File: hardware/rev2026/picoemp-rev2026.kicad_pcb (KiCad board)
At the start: 2 copper layers, 40 x 130 mm, 53 parts, among them J1 EDGE-SMA, J2 1x2_Pin_Header, J3 MKDS 1,5/2-5.08, J4 EDGE-SMA, P1 Header 7, P2 Header 2, P3 Header 4, Q1 LDA111STR, Q2 RGT16BM65DTL, Q3 AO3422, Q4 AO3422, SW1 KSC741J LFS, SW2 KSC741J LFS, SW3 TL3301AF160QJ, T1 ATB322524, T2 ATB322524, U1 SC0915, U2 74LVC1G17

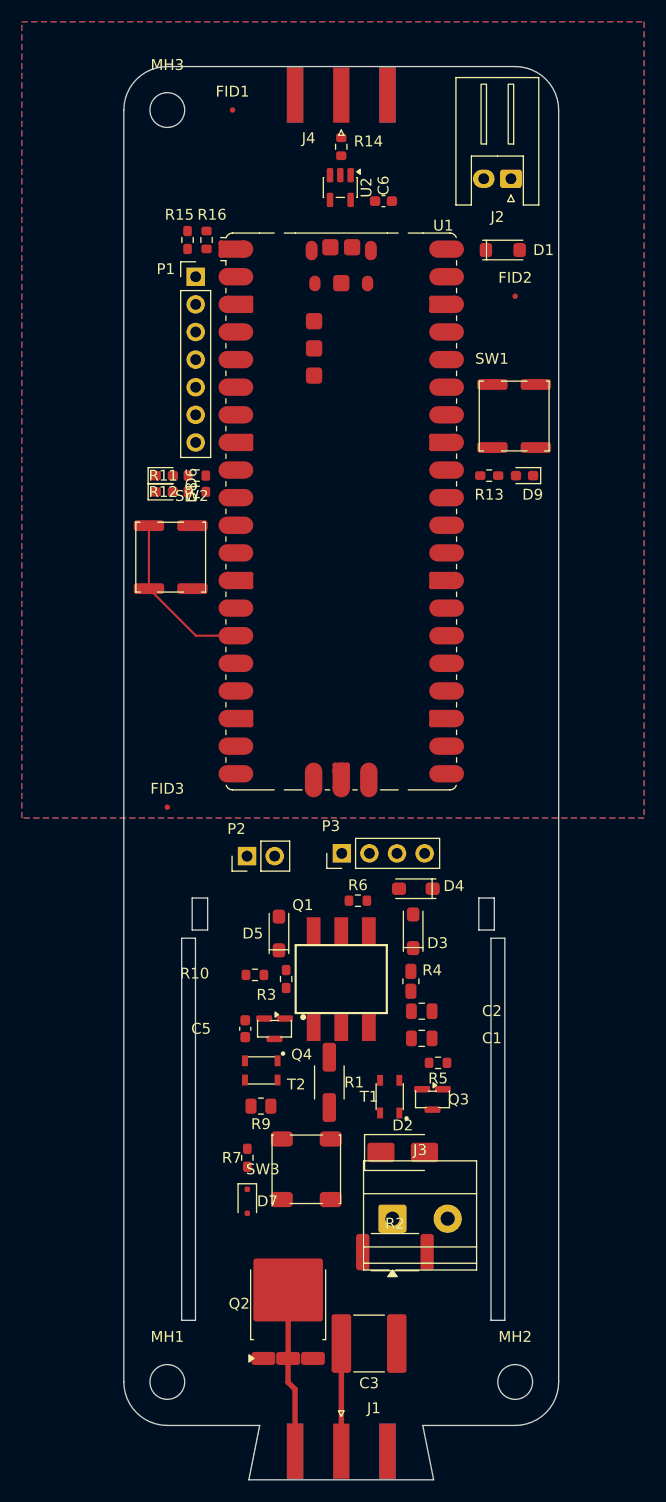
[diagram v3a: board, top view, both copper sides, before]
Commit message: Cut a USB notch in the north edge; J4 east; rearrange the north end
The Pico's USB faces north with 13.6 mm of board in front of it. The connector
centreline sits ~1.5 mm above our board surface, so a micro-B plug body -- ~6 mm
tall, centred -- would need to occupy space 1.5 mm BELOW the board. It cannot be
inserted at all. Moving J4 alone would not have fixed this; the plug is the
problem, not the SMA.

Chose a notch over moving the Pico north. Moving it up sounds cleaner and frees
enough length to shorten the board back toward 116 mm, but the module is 23 mm
wide and the usable north edge is only 32 mm, so the Pico would occupy all but
~4.5 mm at each end and J4 -- which must be at rot +/-90 -- would have nowhere to
go. Pico-north fixes the USB by breaking the trigger SMA. The notch fixes both.

  notch          x 118.39..130.39, y 19.872..33.0   centred on the USB
  west strip     x 108.39..118.39  10.00 mm         R14, U2, C6, D1, MH3, FID1
  east strip     x 130.39..143.12  12.73 mm         J4 (1.36 mm each side), J2

The north-east corner radius drops 4.000 -> 1.270 to make that east strip fit.
R=4.000 exists to be concentric with a mounting hole, and the north-east corner
has none, so it was the only radius that could be conceded without losing what
the radius was for. The other three keep it.

J4 is DNP -- an optional trigger input -- so where the two competed, the USB won
and J4 took the compromise. It still lands with 1.36 mm of margin.

MH3 is NOT centred at the top as asked: that is exactly where the USB notch has
to go. It stays concentric in the north-west corner instead.

Two placement attempts were backed out before this one. Shifting the Pico 1 mm
west to centre the notch on it cascaded into P1/R11/R12/SW2 and shorted SW2 pad 2
to U1 pad 11. Putting the trigger front-end in the east strip left no room for
J2, whose courtyard is 8.4 x 12.5 mm.

DRC back to exactly 7 errors -- every one pre-existing in the HV cluster, none
introduced by this rearrange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
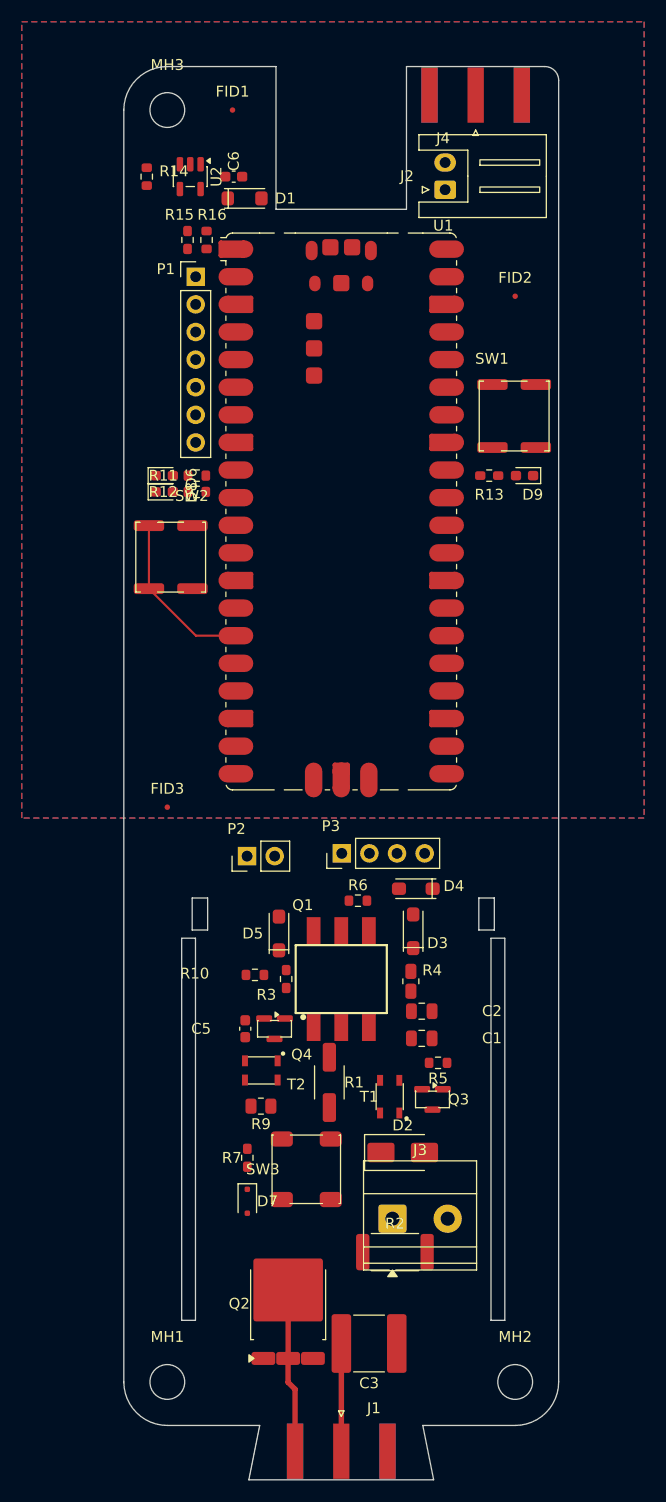
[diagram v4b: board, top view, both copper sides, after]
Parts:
- moved D1 24.2 mm to (115.5, 32.0)
- moved R14 18.1 mm to (106.5, 30.0)
- moved C6 14.0 mm to (114.5, 30.0)
- moved U2 13.8 mm to (110.5, 30.0)
- moved J4 12.4 mm to (136.8, 22.5)
- moved J2 6.14 mm to (133.9, 31.2), turned to 90 degrees
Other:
- outline, holes or cut-outs redrawn
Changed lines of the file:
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@@
 	(footprint "Capacitor_SMD:C_0603_1608Metric"
 		(layer "F.Cu")
-		(at 128.275 32.25)
+		(at 114.5 30)
 		(descr "Capacitor SMD 0603 (1608 Metric), square (rectangular) end terminal, IPC-7351 nominal, (Body size source: IPC-SM-782 page 76, https://www.pcb-3d.com/wordpress/wp-content/uploads/ipc-sm-782a_amendment_1_and_2.pdf)")
 		(tags "capacitor")
@@
 	(footprint "picoemp:D_SOD-123FL"
 		(layer "F.Cu")
-		(at 139.25 36.75)
+		(at 115.5 32)
 		(descr "MCC SOD-123FL (flat lead), e.g. SM4005PL-TP. Pad centres at +/-1.55mm (3.10mm span), size 1.15x1.3mm -- copied from the as-fabricated main:DSS13UTR footprint used for D1 on the original board (a SOD-123FL rectifier), and cross-checked against Central Semiconductor's own SOD-123FL mounting-pad drawing (4.1mm overall pad-to-pad envelope minus a 0.95mm pad width = 3.15mm centre span, within 0.05mm). An earlier draft of this footprint used MCC's suggested-pad-layout figure at 2.36mm; that number turned out to be the INNER-EDGE gap between pads, not the centre-to-centre span, so the earlier pads landed short of the body outline entirely. KiCad's stock Diode_SMD:D_SOD-123F uses a 2.8mm pad span (1.1x1.1mm square pads), which is still off this package's real geometry; use this footprint instead for SOD-123FL parts.")
 		(tags "diode SOD-123FL SOD123FL flat lead")
@@
 	(footprint "Connector_Coaxial:SMA_Amphenol_132289_EdgeMount"
 		(layer "F.Cu")
-		(at 124.39 22.499 90)
+		(at 136.755 22.499 90)
 		(descr "https://www.amphenolrf.com/library/download/link/link_id/595984/parent/132289/")
 		(tags "SMA")
@@
 	(footprint "Connector_JST:JST_XH_S2B-XH-A_1x02_P2.50mm_Horizontal"
 		(layer "F.Cu")
-		(at 140 30.195 180)
+		(at 133.945 31.2 90)
 		(descr "JST XH series connector, S2B-XH-A (http://www.jst-mfg.com/product/pdf/eng/eXH.pdf)")
 		(tags "connector JST XH horizontal")
@@
 	(footprint "Package_TO_SOT_SMD:SOT-23-5"
 		(layer "F.Cu")
-		(at 124.3025 31 -90)
+		(at 110.5 30 -90)
 		(descr "SOT, 5 Pin (JEDEC MO-178 Var AA https://www.jedec.org/document_search?search_api_views_fulltext=MO-178)")
 		(tags "SOT TO_SOT_SMD")
@@
 	(footprint "Resistor_SMD:R_0603_1608Metric"
 		(layer "F.Cu")
-		(at 124.39 27.25 -90)
+		(at 106.5 30 -90)
 		(descr "Resistor SMD 0603 (1608 Metric), square (rectangular) end terminal, IPC-7351 nominal, (Body size source: IPC-SM-782 page 72, https://www.pcb-3d.com/wordpress/wp-content/uploads/ipc-sm-782a_amendment_1_and_2.pdf)")
 		(tags "resistor")
@@
 	)
 	(gr_line
-		(start 140.39 19.872)
+		(start 143.12 19.872)
+		(end 130.39 19.872)
+		(stroke
+			(width 0.05)
+			(type solid)
+		)
+		(layer "Edge.Cuts")
+	)
+	(gr_line
+		(start 130.39 19.872)
+		(end 130.39 33)
+		(stroke
+			(width 0.05)
+			(type solid)
+		)
+		(layer "Edge.Cuts")
+	)
+	(gr_line
+		(start 130.39 33)
+		(end 118.39 33)
+		(stroke
+			(width 0.05)
+			(type solid)
+		)
+		(layer "Edge.Cuts")
+	)
+	(gr_line
+		(start 118.39 33)
+		(end 118.39 19.872)
+		(stroke
+			(width 0.05)
+			(type solid)
+		)
+		(layer "Edge.Cuts")
+	)
+	(gr_line
+		(start 118.39 19.872)
 		(end 108.39 19.872)
 		(stroke
@@
 	)
 	(gr_arc
-		(start 140.39 19.872)
-		(mid 143.2184 21.0436)
-		(end 144.39 23.872)
+		(start 143.1200 19.8720)
+		(mid 144.0180 20.2440)
+		(end 144.3900 21.1420)
 		(stroke
 			(width 0.05)
@@
 	(gr_line
 		(start 144.39 140.872)
-		(end 144.39 23.872)
+		(end 144.39 21.142)
 		(stroke
 			(width 0.05)

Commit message: Fix Q2's pad rotation: 0.080 mm -> 1.080 mm between IGBT leads
The library footprint was never the problem. Package_TO_SOT_SMD:TO-252-3_TabPin2
is correct -- 1.2 mm pads on a 2.286 mm pitch, matching a 0.9 mm DPAK lead.

Pad angles in a .kicad_pcb are ABSOLUTE. Q2's pads carried no angle at all while
its footprint sat at rot 90, so they never rotated with it and presented their
2.2 mm dimension across the 2.286 mm pitch instead of their 1.2 mm one. That is
where 0.080 mm came from. Stamping the footprint's 90 deg onto its eight pads
fixes it; the pads now plot 1.200 mm across the pitch with 1.080 mm gaps, and
Q2's DRC violations are gone.

Those pads are the IGBT gate, collector and emitter. 0.080 mm is close to the
~240 V that gap breaks down at in air and below JLCPCB's 0.127 mm minimum, so
this was a genuine flashover path on a 250 V node, not a tooling artefact.
Leaving the violation visible instead of excluding it was what kept it findable.

Settled by measurement, after reasoning from coordinates gave the wrong answer
twice. SOT-23-5 is the discriminating case: its pads spread along local Y at
0.95 mm pitch with (size 1.325 0.6), so size[1] must be the Y extent -- the
standard (size X Y) reading -- which is what proves the TO-252 library geometry
is right and the board's copy was wrong.

The same root cause explains J4's orientation-dependent short. The SMA library
footprint carries (at 0 0 90) on its pads; the board's copy lost it. At rot 90
that happens to be harmless -- a rectangle is identical under 180 deg -- but at
rot 0 the pads present 5.08 mm across a 4.25 mm pitch and overlap. So J4 CAN go
on the east edge once its pad angles are restored.

An audit flags 22 further footprints whose board pad angles do not match
footprint rotation plus library pad angle. Deliberately NOT bulk-edited: that
model is unvalidated, and this session has already produced two wrong
conclusions from reasoning rather than measuring. Use KiCad's own Update
Footprints from Libra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
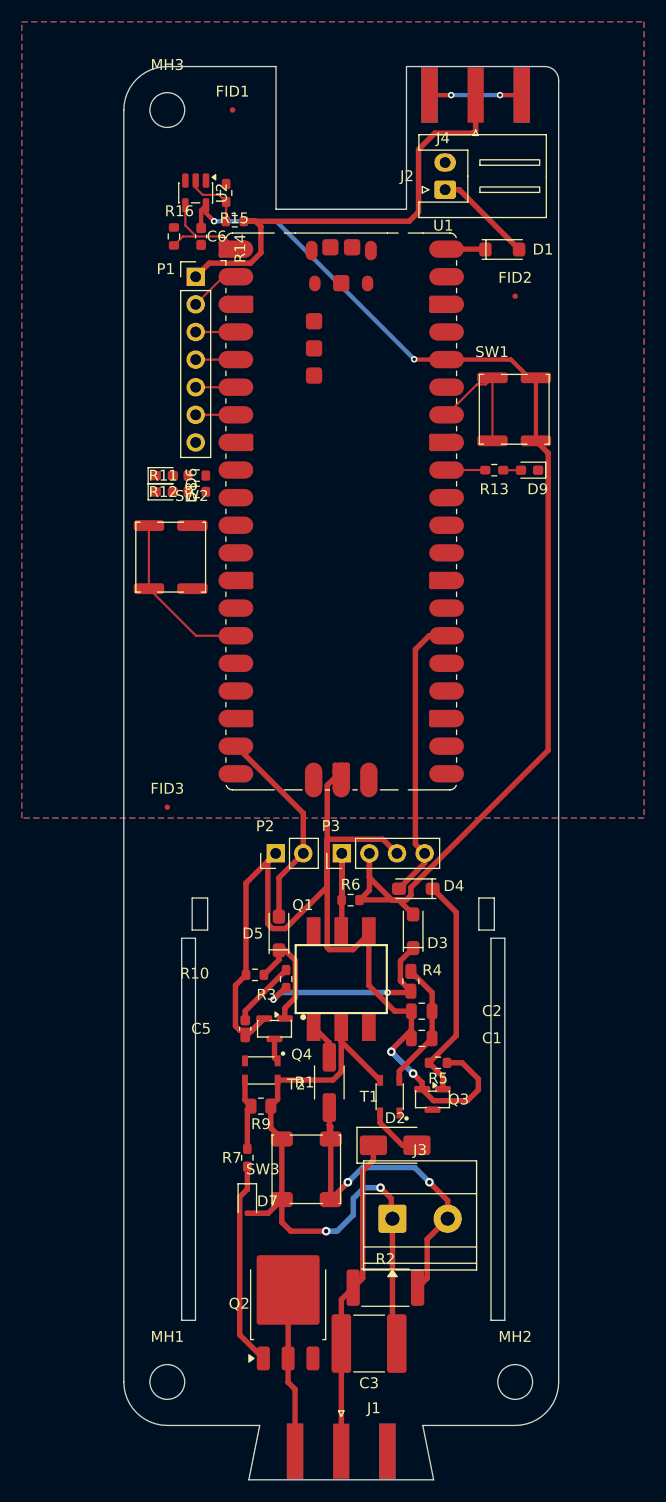
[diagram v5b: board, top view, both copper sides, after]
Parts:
- moved D1 24.2 mm to (139.2, 36.7)
- moved R14 9.08 mm to (114.6, 34.1), turned to 180 degrees
- moved C6 6.26 mm to (111.5, 35.5), turned to -90 degrees
- moved R15 5.60 mm to (113.8, 31.5), turned to 90 degrees
- moved R2 3.39 mm to (128.4, 132.2)
- moved R16 3.02 mm to (109.0, 35.5)
- moved P2 2.65 mm to (118.4, 92.2)
- moved U2 1.58 mm to (111.0, 31.5)
- moved D2 0.96 mm to (129.3, 119.1)
- moved D9 0.68 mm to (141.7, 57.0)
- moved R13 0.68 mm to (138.5, 57.0)
- moved R6 0.68 mm to (125.2, 96.5)
- moved SW1 0.62 mm to (140.3, 51.4)
- turned R1 to 90 degrees
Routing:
- net +3V3: track 0.00 -> 110.1 mm, vias 0 -> 2
- net GND: track 0.00 -> 108.9 mm, vias 0 -> 4
- net /HV_RTN: track 0.00 -> 61.0 mm, vias 0 -> 2
- net /TRIG_IN: track 0.00 -> 42.5 mm
- net /HV_SENSE: track 0.00 -> 32.3 mm, vias 0 -> 2
- net /HVPWM: track 0.00 -> 26.7 mm
- net /Q3_GATE: track 0.00 -> 20.9 mm
- net /HV_RAIL: track 9.91 -> 29.4 mm
- net /PRI_CLAMP: track 0.00 -> 19.4 mm, vias 0 -> 2
- net /HVPULSE: track 0.00 -> 19.2 mm
- net /HV_GATE: track 0.00 -> 18.8 mm
- net /T1_PRI_B: track 0.00 -> 12.1 mm
- net /CHARGED: track 0.00 -> 11.5 mm
- net /ARM_SW: track 0.00 -> 11.4 mm
- net /Q4_GATE: track 0.00 -> 10.5 mm
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
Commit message: Restore DNP attributes wiped by Update Footprints from Library
Update Footprints from Library fixed all 22 remaining pad-rotation mismatches --
the audit now reports zero, and Q2's fix survived intact. It also reset the
board-side "Do not populate" attribute on J4 and R16, which the schematic still
marks dnp=True. Restored, taking schematic parity from 55 issues to 53.

The 53 that remain are all one warning repeated: "Missing symbol field 'DigiKey'
in footprint". Footprints do not carry BOM fields and are not meant to -- the BOM
comes from the schematic, which still has every MPN and DigiKey number. Benign.

Co-Authored-By: Claude Opus 5 <noreply@anthropic.com>
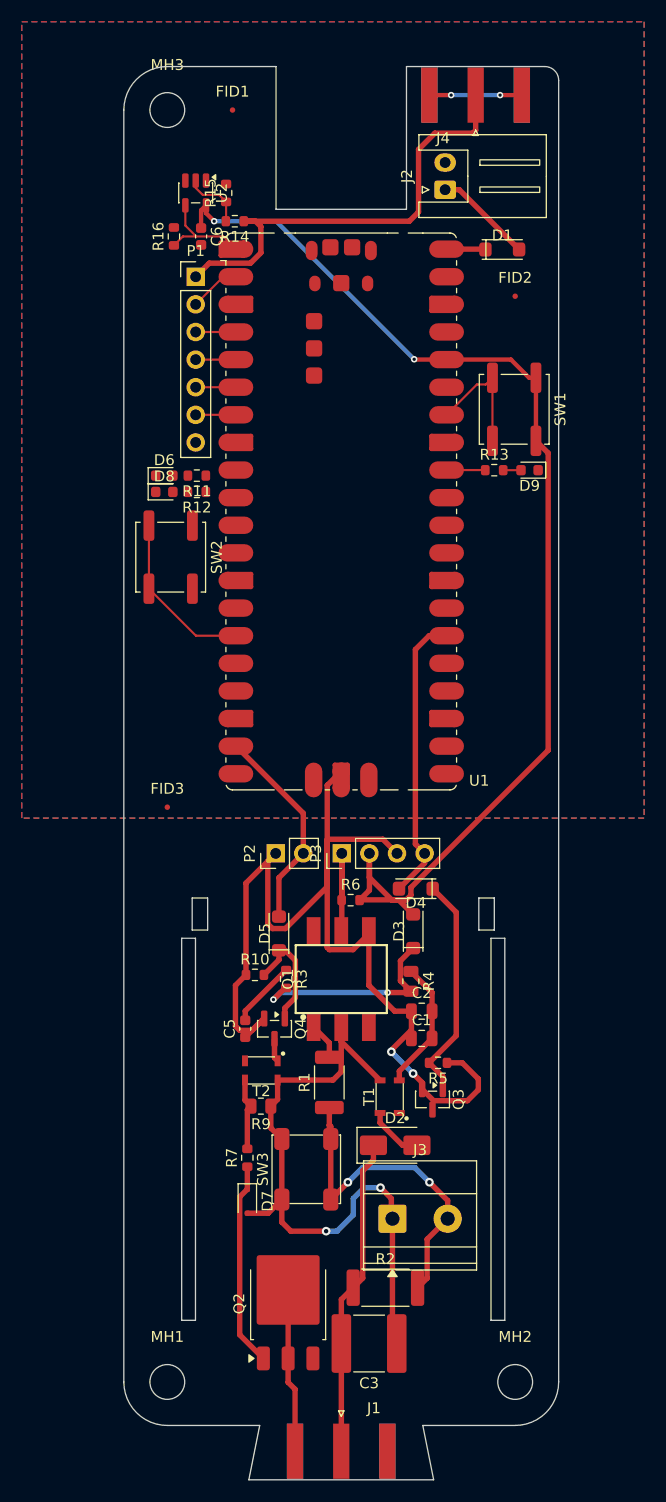
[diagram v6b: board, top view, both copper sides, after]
